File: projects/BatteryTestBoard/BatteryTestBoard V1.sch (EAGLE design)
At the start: 134 parts, among them SW1 BTS50015-1TAD, U1 AP9211SA-AG-HAC-7, U2 AD8418, U3 AD8418, U4 LC05111C13MTTTG, U5 LTC4121

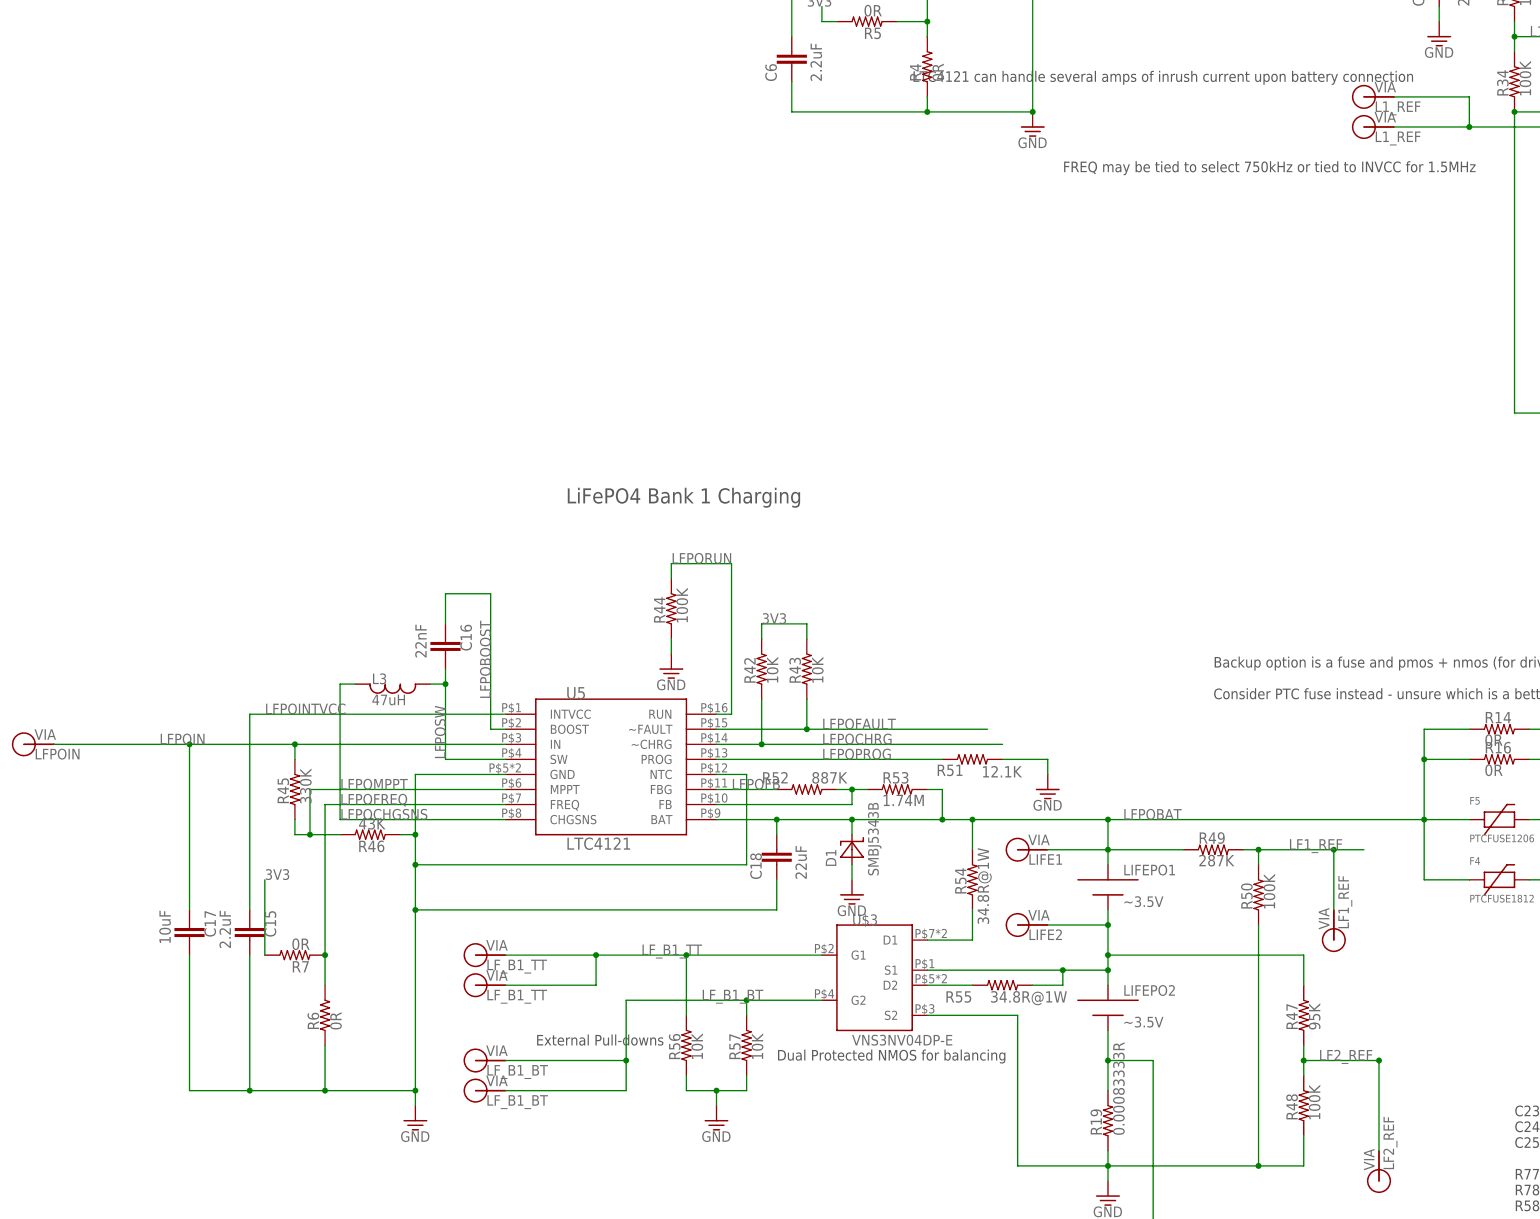
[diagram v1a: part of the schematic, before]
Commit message: Manually routed most of board
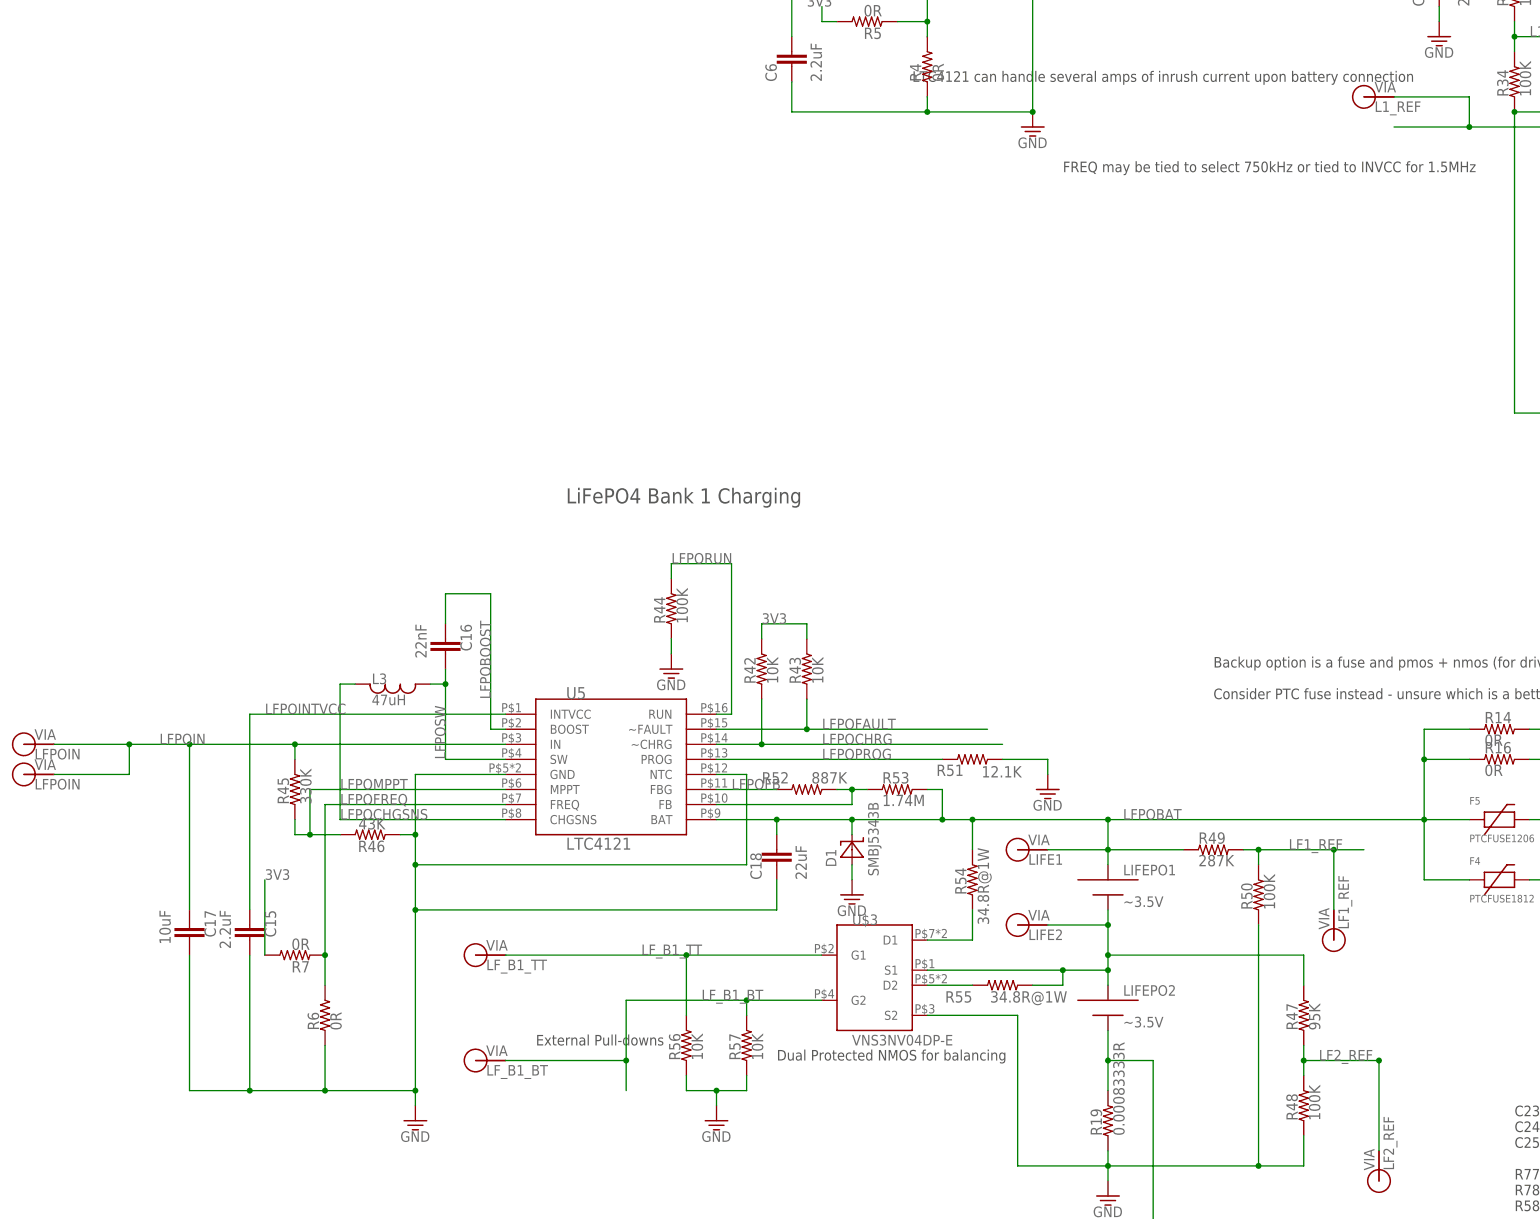
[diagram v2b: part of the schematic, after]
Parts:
- removed V25: L1_REF, BrownSpaceEngineering:VIA-60MIL
- removed V30: LF_B1_TT, BrownSpaceEngineering:VIA60MIL-SQ
- removed V33: LF_B1_BT, BrownSpaceEngineering:VIA60MIL-SQ
- added V9: LFPOIN, BrownSpaceEngineering:VIA60MIL-SQ
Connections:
- removed net N$13: R21.1, U4.S2
- net GND: now also R21.1, U4.S2
- net L1_REF: no longer V25.P$1
- net LFPOIN: now also V9.P$1
- net LF_B1_BT: no longer V33.P$1
- net LF_B1_TT: no longer V30.P$1
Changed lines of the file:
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@@
 <part name="R33" library="BrownSpaceEngineering" deviceset="RES" device="0805" value="150K"/>
 <part name="R34" library="BrownSpaceEngineering" deviceset="RES" device="0805" value="100K"/>
-<part name="V25" library="BrownSpaceEngineering" deviceset="VIA" device="-60MIL" value="L1_REF"/>
 <part name="V43" library="BrownSpaceEngineering" deviceset="VIA" device="60MIL-SQ" value="L1_SNS"/>
 <part name="V44" library="BrownSpaceEngineering" deviceset="VIA" device="60MIL-SQ" value="L1_REF"/>
@@
 <part name="V13" library="BrownSpaceEngineering" deviceset="VIA" device="60MIL-SQ" value="LIFEB1SNS"/>
 <part name="V29" library="BrownSpaceEngineering" deviceset="VIA" device="60MIL-SQ" value="LF_B1_TT"/>
-<part name="V30" library="BrownSpaceEngineering" deviceset="VIA" device="60MIL-SQ" value="LF_B1_TT"/>
 <part name="V32" library="BrownSpaceEngineering" deviceset="VIA" device="60MIL-SQ" value="LF_B1_BT"/>
-<part name="V33" library="BrownSpaceEngineering" deviceset="VIA" device="60MIL-SQ" value="LF_B1_BT"/>
 <part name="V34" library="BrownSpaceEngineering" deviceset="VIA" device="60MIL-SQ" value="LIONIN"/>
 <part name="V35" library="BrownSpaceEngineering" deviceset="VIA" device="60MIL-SQ" value="LIONIN"/>
@@
 <part name="V41" library="BrownSpaceEngineering" deviceset="VIA" device="60MIL-SQ" value="GND"/>
 <part name="R22" library="BrownSpaceEngineering" deviceset="RES" device="1210" value="0R"/>
+<part name="V9" library="BrownSpaceEngineering" deviceset="VIA" device="60MIL-SQ" value="LFPOIN"/>
 </parts>
 <sheets>
@@
 <instance part="R33" gate="R$1" x="149.86" y="93.98" rot="R90"/>
 <instance part="R34" gate="R$1" x="149.86" y="78.74" rot="R90"/>
-<instance part="V25" gate="G$1" x="124.46" y="71.12"/>
 <instance part="V43" gate="G$1" x="304.8" y="50.8" rot="R90"/>
 <instance part="V44" gate="G$1" x="124.46" y="76.2"/>
@@
 <instance part="V13" gate="G$1" x="154.94" y="-154.94" rot="R90"/>
 <instance part="V29" gate="G$1" x="-25.4" y="-68.58"/>
-<instance part="V30" gate="G$1" x="-25.4" y="-73.66"/>
 <instance part="V32" gate="G$1" x="-25.4" y="-86.36"/>
-<instance part="V33" gate="G$1" x="-25.4" y="-91.44"/>
 <instance part="V34" gate="G$1" x="-27.94" y="106.68"/>
 <instance part="V35" gate="G$1" x="-27.94" y="114.3"/>
@@
 <instance part="V41" gate="G$1" x="248.92" y="-12.7" rot="R180"/>
 <instance part="R22" gate="R$1" x="269.24" y="119.38"/>
+<instance part="V9" gate="G$1" x="-101.6" y="-38.1"/>
 </instances>
 <busses>
@@
 <junction x="-50.8" y="-91.44"/>
 </segment>
+<segment>
+<wire x1="182.88" y1="55.88" x2="167.64" y2="55.88" width="0.1524" layer="91"/>
+<wire x1="167.64" y1="55.88" x2="167.64" y2="38.1" width="0.1524" layer="91"/>
+<pinref part="R21" gate="R$1" pin="1"/>
+<wire x1="167.64" y1="38.1" x2="167.64" y2="35.56" width="0.1524" layer="91"/>
+<wire x1="172.72" y1="40.64" x2="172.72" y2="38.1" width="0.1524" layer="91"/>
+<wire x1="172.72" y1="38.1" x2="167.64" y2="38.1" width="0.1524" layer="91"/>
+<junction x="167.64" y="38.1"/>
+<pinref part="U4" gate="G$1" pin="S2"/>
+<pinref part="GND5" gate="1" pin="GND"/>
+</segment>
 </net>
 <net name="LIONCHRG" class="0">
@@
 <wire x1="162.56" y1="86.36" x2="157.48" y2="86.36" width="0.1524" layer="91"/>
 <junction x="149.86" y="86.36"/>
-<pinref part="V25" gate="G$1" pin="P$1"/>
 <wire x1="157.48" y1="86.36" x2="149.86" y2="86.36" width="0.1524" layer="91"/>
 <wire x1="129.54" y1="71.12" x2="142.24" y2="71.12" width="0.1524" layer="91"/>
@@
 <wire x1="0" y1="-86.36" x2="0" y2="-76.2" width="0.1524" layer="91"/>
 <wire x1="0" y1="-76.2" x2="20.32" y2="-76.2" width="0.1524" layer="91"/>
-<pinref part="V33" gate="G$1" pin="P$1"/>
-<wire x1="-20.32" y1="-91.44" x2="0" y2="-91.44" width="0.1524" layer="91"/>
 <wire x1="0" y1="-91.44" x2="0" y2="-86.36" width="0.1524" layer="91"/>
 <junction x="0" y="-86.36"/>
@@
 <junction x="10.16" y="-68.58"/>
 <label x="2.54" y="-68.58" size="1.778" layer="95"/>
-<wire x1="10.16" y1="-68.58" x2="-5.08" y2="-68.58" width="0.1524" layer="91"/>
 <pinref part="V29" gate="G$1" pin="P$1"/>
-<wire x1="-5.08" y1="-68.58" x2="-20.32" y2="-68.58" width="0.1524" layer="91"/>
-<wire x1="-5.08" y1="-68.58" x2="-5.08" y2="-73.66" width="0.1524" layer="91"/>
-<junction x="-5.08" y="-68.58"/>
-<pinref part="V30" gate="G$1" pin="P$1"/>
-<wire x1="-5.08" y1="-73.66" x2="-20.32" y2="-73.66" width="0.1524" layer="91"/>
+<wire x1="10.16" y1="-68.58" x2="-20.32" y2="-68.58" width="0.1524" layer="91"/>
 </segment>
 </net>
@@
 <junction x="-73.66" y="-33.02"/>
 <pinref part="V75" gate="G$1" pin="P$1"/>
-<wire x1="-73.66" y1="-33.02" x2="-96.52" y2="-33.02" width="0.1524" layer="91"/>
+<wire x1="-73.66" y1="-33.02" x2="-83.82" y2="-33.02" width="0.1524" layer="91"/>
+<pinref part="V9" gate="G$1" pin="P$1"/>
+<wire x1="-83.82" y1="-33.02" x2="-96.52" y2="-33.02" width="0.1524" layer="91"/>
+<wire x1="-96.52" y1="-38.1" x2="-83.82" y2="-38.1" width="0.1524" layer="91"/>
+<wire x1="-83.82" y1="-38.1" x2="-83.82" y2="-33.02" width="0.1524" layer="91"/>
+<junction x="-83.82" y="-33.02"/>
 </segment>
 </net>
@@
 </segment>
 </net>
-<net name="N$13" class="0">
-<segment>
-<wire x1="182.88" y1="55.88" x2="167.64" y2="55.88" width="0.1524" layer="91"/>
-<wire x1="167.64" y1="55.88" x2="167.64" y2="38.1" width="0.1524" layer="91"/>
-<pinref part="R21" gate="R$1" pin="1"/>
-<wire x1="167.64" y1="38.1" x2="167.64" y2="35.56" width="0.1524" layer="91"/>
-<wire x1="172.72" y1="40.64" x2="172.72" y2="38.1" width="0.1524" layer="91"/>
-<wire x1="172.72" y1="38.1" x2="167.64" y2="38.1" width="0.1524" layer="91"/>
-<junction x="167.64" y="38.1"/>
-<pinref part="U4" gate="G$1" pin="S2"/>
-</segment>
-</net>

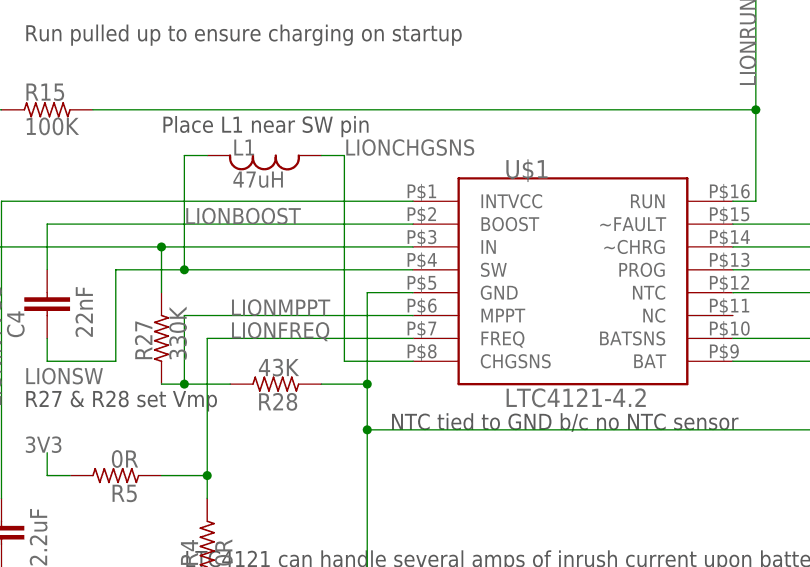
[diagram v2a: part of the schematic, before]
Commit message: Routed board
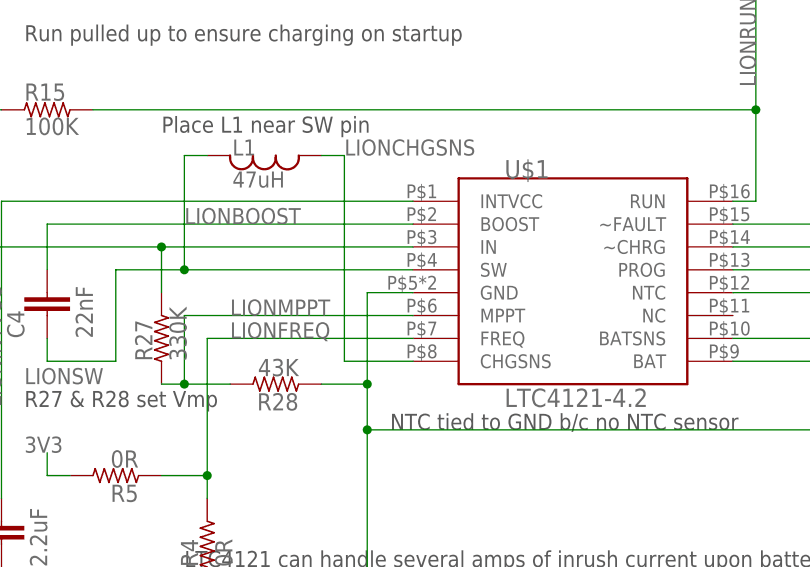
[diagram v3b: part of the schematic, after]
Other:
- moved on the sheet: U$1

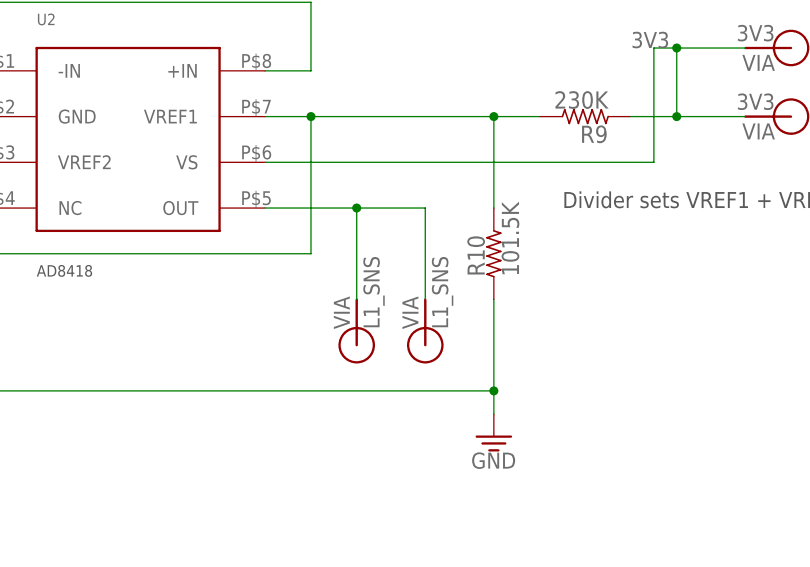
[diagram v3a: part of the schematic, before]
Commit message: Silkscreen information
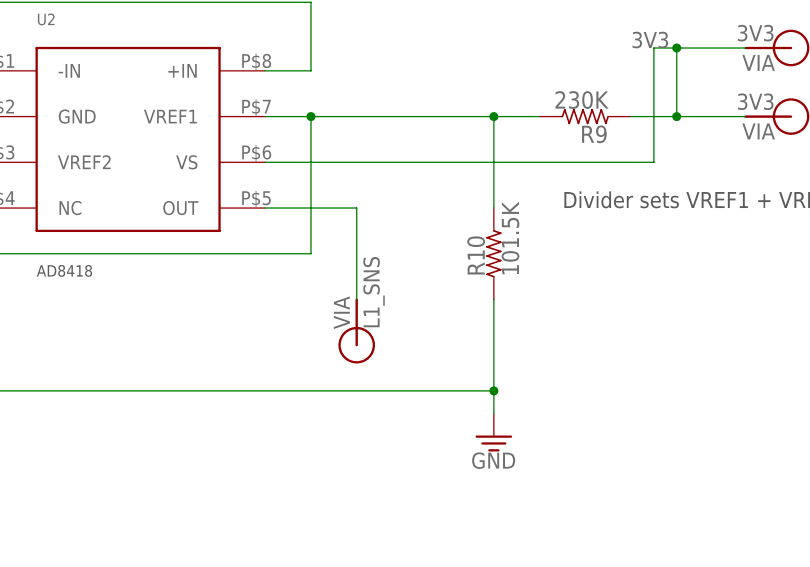
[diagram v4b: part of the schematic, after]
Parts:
- removed V2: L1_SNS, BrownSpaceEngineering:VIA60MIL-SQ
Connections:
- net L1_SNS: no longer V2.P$1
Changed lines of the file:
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@@
 <part name="V59" library="BrownSpaceEngineering" deviceset="VIA" device="60MIL-SQ" value="LF2_REF"/>
 <part name="U$1" library="BrownSpaceEngineering" deviceset="LTC4121-4.2" device=""/>
-<part name="V2" library="BrownSpaceEngineering" deviceset="VIA" device="60MIL-SQ" value="L1_SNS"/>
 <part name="V5" library="BrownSpaceEngineering" deviceset="VIA" device="60MIL-SQ" value="GND"/>
 <part name="V6" library="BrownSpaceEngineering" deviceset="VIA" device="60MIL-SQ" value="GND"/>
@@
 <instance part="V59" gate="G$1" x="127" y="-106.68" rot="R90"/>
 <instance part="U$1" gate="G$1" x="86.36" y="111.76"/>
-<instance part="V2" gate="G$1" x="312.42" y="50.8" rot="R90"/>
 <instance part="V5" gate="G$1" x="248.92" y="17.78" rot="R180"/>
 <instance part="V6" gate="G$1" x="248.92" y="12.7" rot="R180"/>
@@
 <pinref part="V43" gate="G$1" pin="P$1"/>
 <wire x1="304.8" y1="55.88" x2="304.8" y2="66.04" width="0.1524" layer="91"/>
-<pinref part="V2" gate="G$1" pin="P$1"/>
-<wire x1="304.8" y1="66.04" x2="312.42" y2="66.04" width="0.1524" layer="91"/>
-<wire x1="312.42" y1="66.04" x2="312.42" y2="55.88" width="0.1524" layer="91"/>
 <wire x1="304.8" y1="66.04" x2="294.64" y2="66.04" width="0.1524" layer="91"/>
-<junction x="304.8" y="66.04"/>
 <pinref part="U2" gate="G$1" pin="OUT"/>
 </segment>

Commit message: Incorporated majority of comments on trello card
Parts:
- removed U$1: LTC4121-4.2, BrownSpaceEngineering:LTC4121-4.2
- added D2: SMBJ5343B, BattBoard:SMBJ5343B
- added M1: (no value), BrownSpaceEngineering:AON7522E
- added M2: IPB120P04P4L03ATMA1, BattBoard:IPB120P04P4L03ATMA1
- added U6: AP9211SA-AG-HAC-7, BattBoard:AP9211SA-AG-HAC-7
- added V2: FUSE_OUT, BrownSpaceEngineering:VIA60MIL-SQ
- F1, F5: value PTCFUSE1206 -> 1206L150THWR; device BattBoard:PTCFUSE1206 -> BattBoard:1206L150THWR
- F4: value PTCFUSE1812 -> MINISMDC200F-2; device BattBoard:PTCFUSE1812 -> BattBoard:MINISMDC200F-2
- R17, R18: value 10K -> 100K
- R8: device BrownSpaceEngineering:RES0805 -> BrownSpaceEngineering:RES1210
- U1: value AP9211SA-AG-HAC-7 -> LTC4121-4.2; device BattBoard:AP9211SA-AG-HAC-7 -> BrownSpaceEngineering:LTC4121-4.2
- V34, V35: value LIONIN -> LION_IN
- V51: value LIONCHRG -> !LIONCHRG
- V52: value LIONFAULT -> !LIONFAULT
- V75, V9: value LFPOIN -> LFPO_IN
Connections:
- net LFPOCHRG renamed !LFPOCHRG
- net LFPOFAULT renamed !LFPOFAULT
- net LFPOIN renamed LFPO_IN
- net VIN+ renamed LIONSNS+
- net VIN+1 renamed LFPOSNS+
- removed net LF_B2: F4.P$2, F5.P$2, R14.2, R16.2, SW1.VB
- removed net LIONCHRG: R17.1, U$1.~CHRG, V51.P$1
- removed net LIONFAULT: R18.1, U$1.~FAULT, V52.P$1
- removed net LIONIN: C3.P$1, R15.1, R27.2, U$1.IN, V34.P$1, V35.P$1
- new net !LIONCHRG: R17.1, U1.~CHRG, V51.P$1
- new net !LIONFAULT: R18.1, U1.~FAULT, V52.P$1
- new net FUSE_OUT: D2.C, F4.P$2, F5.P$2, M2.D, R14.2, R16.2, SW1.VB, V2.P$1
- new net LION_IN: C3.P$1, R15.1, R27.2, U1.IN, V34.P$1, V35.P$1
- new net N$7: M1.D, M2.G
- net GND: now also D2.A, M1.S, U1.GND, U1.NTC, U6.S2; no longer U$1.GND, U$1.NTC, U1.S2
- net LF_B1_OUTEN: now also M1.G
- net LIONBAT: now also U1.BAT, U1.BATSNS; no longer U$1.BAT, U$1.BATSNS
- net LIONBOOST: now also U1.BOOST; no longer U$1.BOOST
- net LIONCHGSNS: now also U1.CHGSNS; no longer U$1.CHGSNS
- net LIONFREQ: now also U1.FREQ; no longer U$1.FREQ
- net LIONINTVCC: now also U1.INTVCC; no longer U$1.INTVCC
- net LIONMPPT: now also U1.MPPT; no longer U$1.MPPT
- net LIONPROG: now also U1.PROG; no longer U$1.PROG
- net LIONRUN: now also U1.RUN; no longer U$1.RUN
- net LIONSW: now also U1.SW; no longer U$1.SW
- net N$1: now also U6.VM; no longer U1.VM
- net N$4: now also U6.S1, U6.VSS; no longer U1.S1, U1.VSS
- net N$5: now also U6.VDD; no longer U1.VDD
- net N$6: now also M2.S
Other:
- note added: "AON7522E"
- note added: "Connect BATSNS close to battery terminal"
- note added: "Either R22 and R13 or the PTC fuse to be soldered"
- note added: "FREQ may be tied to GND select 750kHz or tied to 3V3 for 1.5MHz. Solder R4 for GND or R5 for 3V3"
- note added: "FREQ may be tied to GND select 750kHz or tied to 3V3 for 1.5MHz. Solder R6 for GND or R7 for 3V3"
- note added: "Loss of inductive load protection"
- note added: "Only one of U4 and U6 to be soldered"
- note added: "R25 sets Ichg=100mA"
- note added: "Solder either NMOS + PMOS or BTS50015-1TAD"
- note added: "Solder either the two 0R resistors Or one of the PTC fuses"
- note removed: "Backup option is a fuse and pmos + nmos (for driving) Consider PTC fuse instead - unsure which is a better option right now."
- note removed: "FREQ may be tied to select 750kHz or tied to INVCC for 1.5MHz"
- note removed: "R21 sets Ichg=100mA"
- moved on the sheet: C23, C24, C25, R58, R77, R78, R79, SW1
